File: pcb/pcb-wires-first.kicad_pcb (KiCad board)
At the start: 2 copper layers, 110 x 70 mm, 52 parts, among them J1 Conn_01x04, J2 Conn_01x04, J3 Conn_01x04, J4 Conn_01x02, J5 Conn_01x02, J6 Conn_01x02, J7 Conn_01x02, SW1 on-1, SW2 off-1, SW3 on-2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

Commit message: More routing.
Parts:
- moved C16 4.27 mm to (139.5, 113.0), turned to -90 degrees
- moved D5 2.00 mm to (161.5, 107.0)
- moved D6 2.00 mm to (161.5, 105.0)
- moved R5 2.00 mm to (158.0, 107.0)
- moved R6 2.00 mm to (158.0, 105.0)
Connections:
- R4 pad 1: switch-3 -> fault
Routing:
- net HV-GND: track 86.0 -> 0.00 mm
- net switch-1: track 33.9 -> 72.0 mm, vias 1 -> 2
- net HV-VDD: track 14.8 -> 43.4 mm
- net fault: track 0.00 -> 24.8 mm
- net switch-3: track 37.3 -> 44.8 mm, vias 1 -> 3
- net switch-2: track 36.0 -> 39.6 mm, vias 1 -> 2
- net Net-(D6-A): track 0.00 -> 1.89 mm
- net Net-(D5-A): track 0.00 -> 1.89 mm
- net /on-2b: track 74.6 -> 76.2 mm
- net /output-2: track 23.9 -> 23.2 mm, vias 0 -> 2
- net /output-3: track 28.2 -> 28.0 mm, vias 0 -> 2
- net /output-1: vias 0 -> 2

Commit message: Routed!
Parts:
- added JP1: SolderJumper_2_Bridged, Jumper:SolderJumper-2_P1.3mm_Bridged_RoundedPad1.0x1.5mm, F.Cu at (152.0, 102.0)
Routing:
- net 3V3: track 2.56 -> 128.9 mm, vias 0 -> 5
- net HV-GND: track 0.00 -> 112.4 mm
- net fault: track 24.8 -> 93.7 mm, vias 0 -> 3
- net switch-2: track 39.6 -> 96.7 mm, vias 2 -> 3
- net switch-3: track 44.8 -> 100.8 mm
- net switch-1: track 72.0 -> 97.0 mm, vias 2 -> 3
- net HV-VDD: track 43.4 -> 60.9 mm
- net GND: track 0.00 -> 4.93 mm, vias 0 -> 15
- net /off-1b: track 76.1 -> 75.0 mm
- net /hv-in-1: vias 1 -> 0
- added copper zone on B.Cu, net GND
- added copper zone on F.Cu, net GND

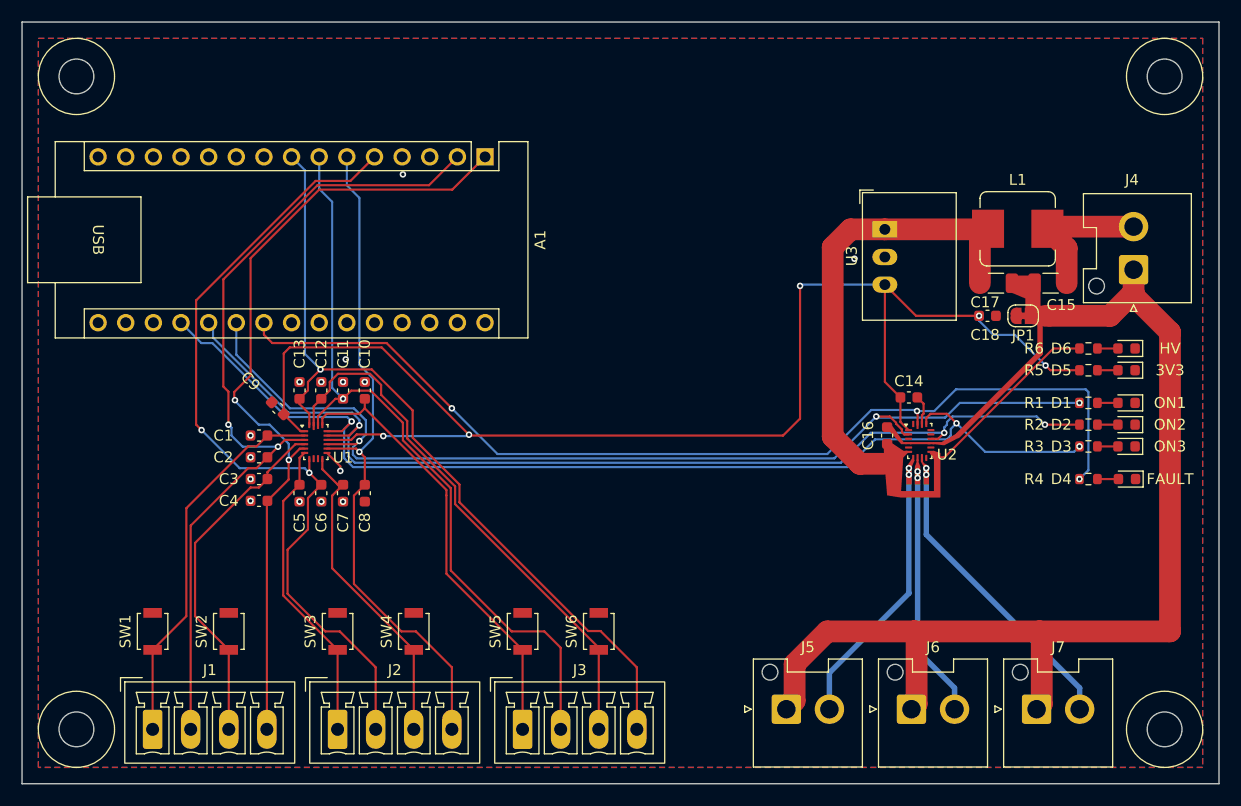
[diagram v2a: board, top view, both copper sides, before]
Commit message: Adding an I2C connector.
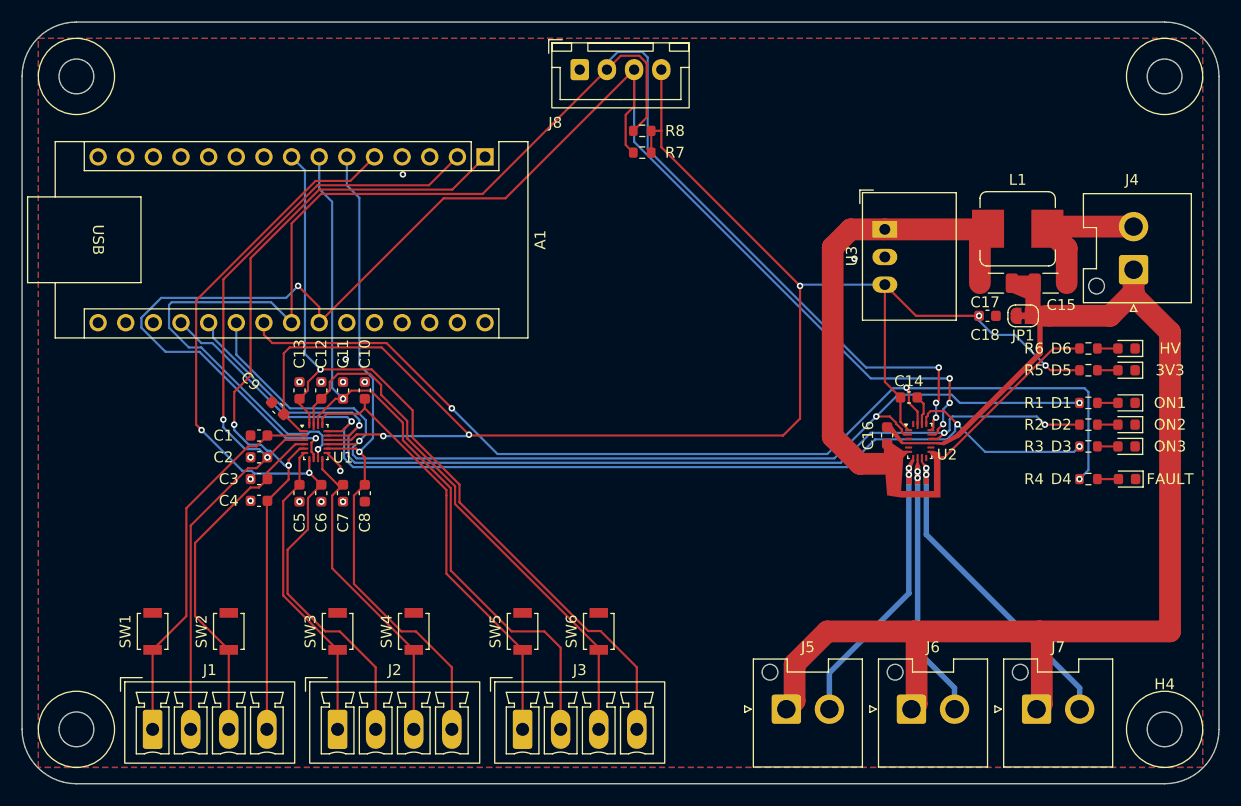
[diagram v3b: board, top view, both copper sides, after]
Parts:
- added J8: Conn_01x04, Connector_JST:JST_XH_B4B-XH-A_1x04_P2.50mm_Vertical, F.Cu at (111.2, 79.4)
- added R7: 4.7k, Resistor_SMD:R_0603_1608Metric, F.Cu at (117.0, 87.0)
- added R8: 4.7k, Resistor_SMD:R_0603_1608Metric, F.Cu at (117.0, 85.0)
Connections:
- A1 pad 23: unconnected-(A1-SDA/A4-Pad23) -> SDA
- A1 pad 24: unconnected-(A1-SCL/A5-Pad24) -> SCL
- U1 pad 8: unconnected-(U1-SCL-Pad8) -> SCL
- U1 pad 9: unconnected-(U1-SDA-Pad9) -> SDA
- U2 pad 15: unconnected-(U2-SCL-Pad15) -> SCL
- U2 pad 16: unconnected-(U2-SDA-Pad16) -> SDA
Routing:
- net SDA: track 0.00 -> 144.6 mm, vias 0 -> 4
- net SCL: track 0.00 -> 140.6 mm, vias 0 -> 5
- net 3V3: track 128.9 -> 157.0 mm
- net fault: track 93.7 -> 96.3 mm
- net /off-1b: track 75.0 -> 75.9 mm
- net /on-1b: track 78.0 -> 77.4 mm
- net switch-1: track 97.0 -> 97.6 mm
- net GND: vias 15 -> 14
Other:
- outline, holes or cut-outs redrawn

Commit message: Doing a draft release.
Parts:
- J5, J6, J7: footprint Connector_JST:JST_VH_B2P-VH-FB-B_1x02_P3.96mm_Vertical -> Connector_JST:JST_VH_B2P-VH_1x02_P3.96mm_Vertical
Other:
- board text added: "Copyright (c) devbotas Wires-first v0.1.0"
